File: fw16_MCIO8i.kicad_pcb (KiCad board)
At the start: 4 copper layers, 118.7 x 72.5 mm, 12 parts

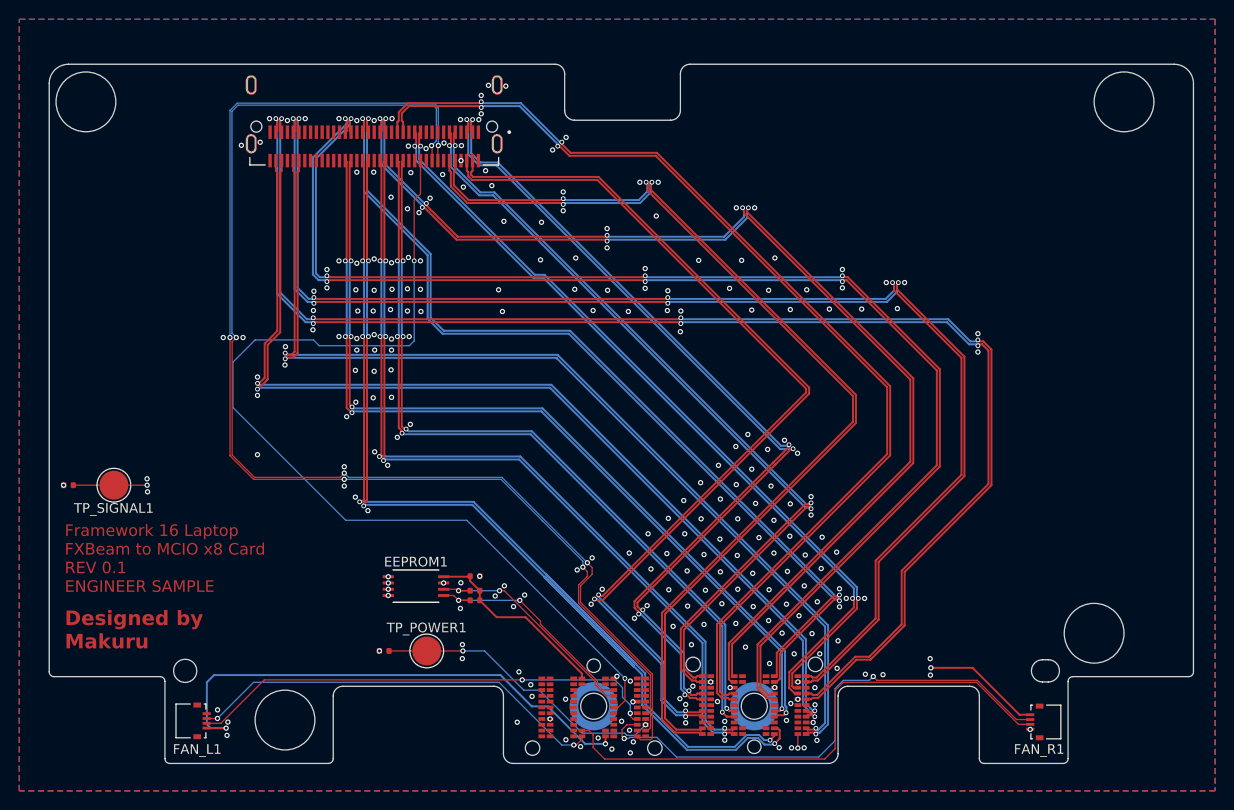
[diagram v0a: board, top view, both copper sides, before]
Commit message: Removed pour on signal layers
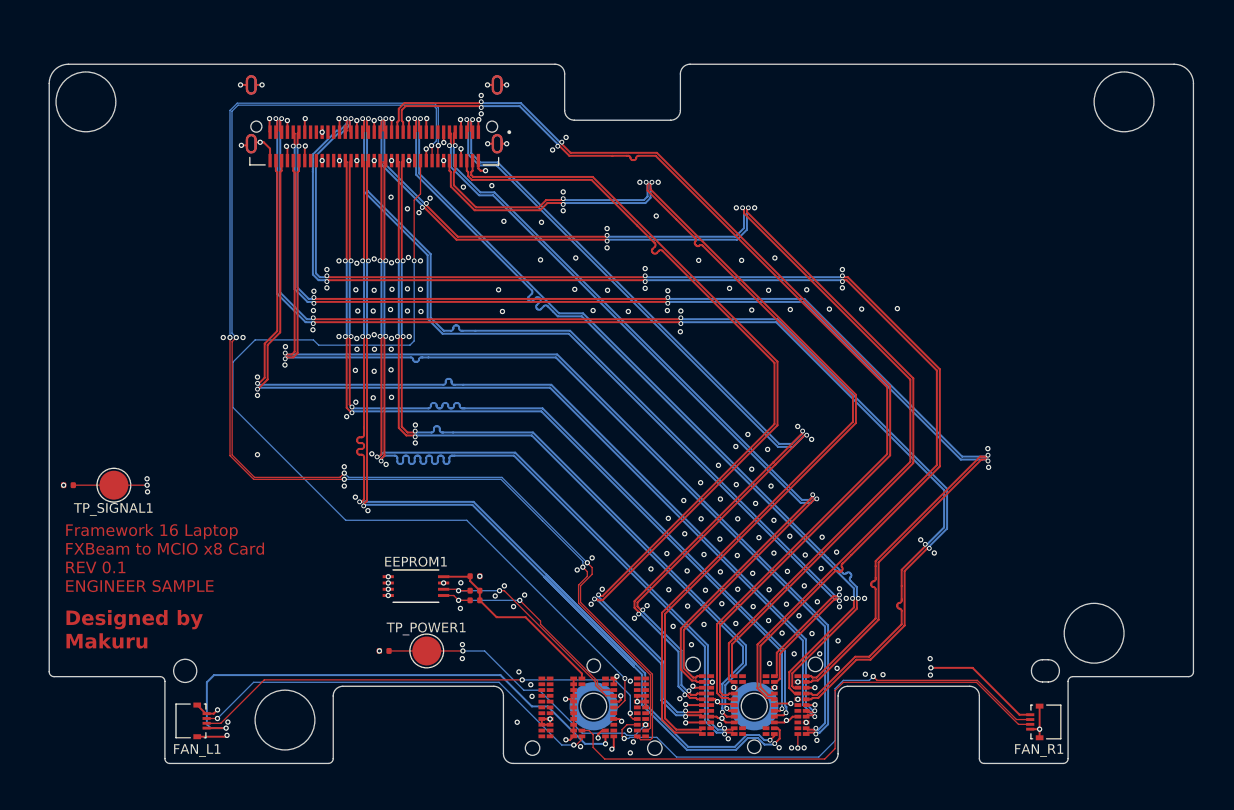
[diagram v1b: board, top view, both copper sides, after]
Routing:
- net GND: track 0.00 -> 80.4 mm, vias 263 -> 269
- net /RX7+: track 141.9 -> 126.9 mm
- net /RX7-: track 141.4 -> 126.9 mm
- net /RX6-: track 135.8 -> 127.9 mm
- net /TX3+: track 84.6 -> 91.4 mm
- net /PEX_CLK-: track 81.2 -> 88.1 mm
- net /RX6+: track 134.2 -> 127.9 mm
- net /PEX_CLK+: track 80.6 -> 84.9 mm
- net /RX0+: track 87.4 -> 91.4 mm
- net /RX0-: track 87.6 -> 91.4 mm
- net /TX0+: track 96.1 -> 93.1 mm
- net /TX2+: track 79.6 -> 82.3 mm
- net /TX5+: track 89.0 -> 91.0 mm
- net /TX4-: track 118.7 -> 120.6 mm
- net /TX0-: track 94.9 -> 93.0 mm
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- removed copper zone on B.Cu, net GND
- removed copper zone on F.Cu, net GND

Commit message: diodes and jumpers
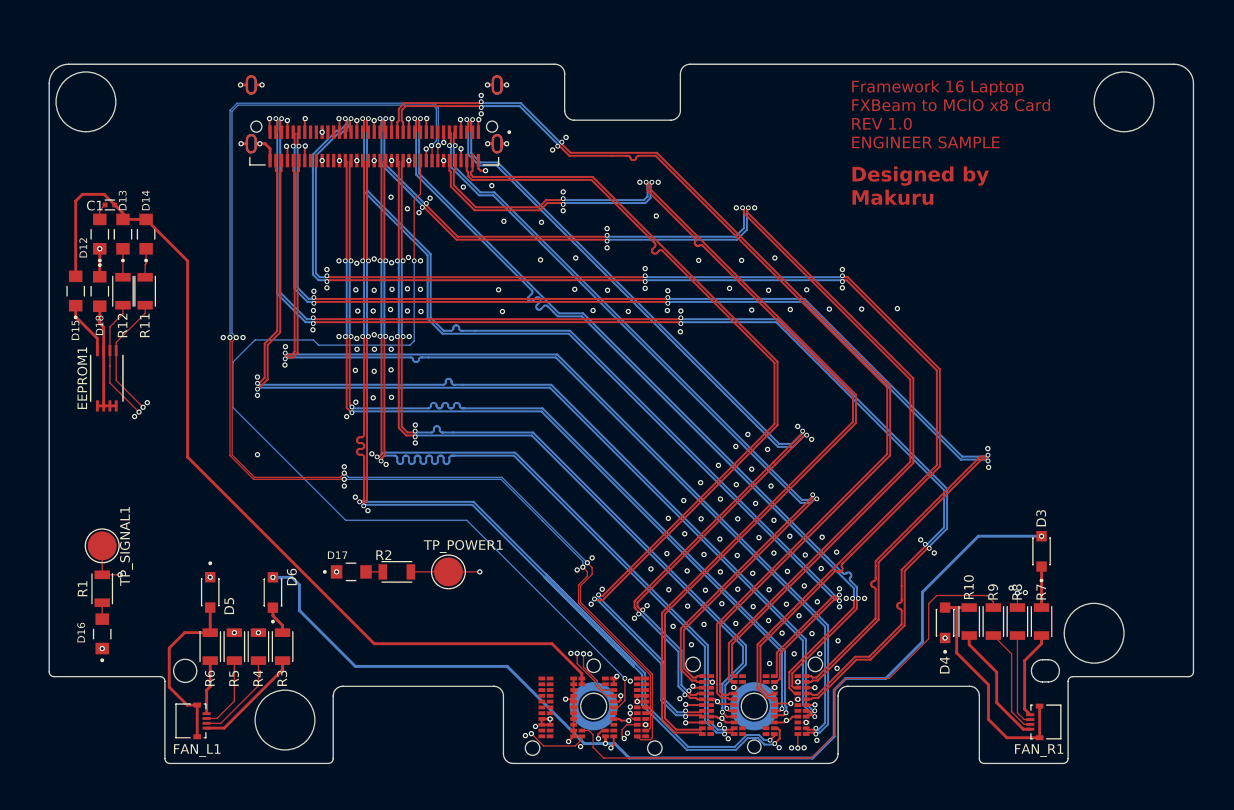
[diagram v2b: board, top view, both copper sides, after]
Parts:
- removed R50, R51: 10kΩ, PCM_JLCPCB:R_0402
- added D12: SS115LW, diode:DIO_SS115LW, F.Cu at (48.3, 42.3)
- added D13: SS115LW, diode:DIO_SS115LW, F.Cu at (50.7, 42.3)
- added D14: SS115LW, diode:DIO_SS115LW, F.Cu at (53.1, 42.3)
- added D15: SS115LW, diode:DIO_SS115LW, F.Cu at (45.8, 48.2)
- added D16: SS115LW, diode:DIO_SS115LW, F.Cu at (48.6, 83.8)
- added D17: SS115LW, diode:DIO_SS115LW, F.Cu at (74.4, 77.3)
- added D18: SS115LW, diode:DIO_SS115LW, F.Cu at (48.3, 48.2)
- added D3: ES15DLW, fan-diode:SODFL3718X102N, F.Cu at (146.0, 75.2)
- added D4: ES15DLW, fan-diode:SODFL3718X102N, F.Cu at (136.0, 82.6)
- added D5: ES15DLW, fan-diode:SODFL3718X102N, F.Cu at (59.8, 79.4)
- added D6: ES15DLW, fan-diode:SODFL3718X102N, F.Cu at (66.3, 79.4)
- added R10: 1206_R_560112132007, resistors:R_Wurth_WRIS-RSKS-1206_R, F.Cu at (138.5, 82.5)
- added R11: 1206_R_560112132018, resistors:R_Wurth_WRIS-RSKS-1206_R, F.Cu at (53.0, 48.2)
- added R12: 1206_R_560112132018, resistors:R_Wurth_WRIS-RSKS-1206_R, F.Cu at (50.7, 48.2)
- added R3: 1206_R_560112132007, resistors:R_Wurth_WRIS-RSKS-1206_R, F.Cu at (67.3, 85.0)
- added R4: 1206_R_560112132007, resistors:R_Wurth_WRIS-RSKS-1206_R, F.Cu at (64.8, 85.0)
- added R5: 1206_R_560112132007, resistors:R_Wurth_WRIS-RSKS-1206_R, F.Cu at (62.3, 85.0)
- added R6: 1206_R_560112132007, resistors:R_Wurth_WRIS-RSKS-1206_R, F.Cu at (59.8, 85.0)
- added R7: 1206_R_560112132007, resistors:R_Wurth_WRIS-RSKS-1206_R, F.Cu at (146.0, 82.5)
- added R8: 1206_R_560112132007, resistors:R_Wurth_WRIS-RSKS-1206_R, F.Cu at (143.5, 82.5)
- added R9: 1206_R_560112132007, resistors:R_Wurth_WRIS-RSKS-1206_R, F.Cu at (141.0, 82.5)
- C1: value 1uF -> 0402_885012105012; footprint PCM_JLCPCB:C_0402 -> capacitor:C_Wurth_WCAP-CSGP-0402
- R1: renamed from R2; value 330kΩ -> 1206_R_560112132036; footprint PCM_JLCPCB:R_0402 -> resistors:R_Wurth_WRIS-RSKS-1206_R
- R2: renamed from R1; value 330kΩ -> 1206_R_560112132036; footprint PCM_JLCPCB:R_0402 -> resistors:R_Wurth_WRIS-RSKS-1206_R
- moved C1 54.0 mm to (49.4, 39.2), turned to 180 degrees
- moved EEPROM1 38.6 mm to (49.1, 57.2), turned to 90 degrees
- moved R1 11.3 mm to (48.6, 79.0), turned to 90 degrees
- moved TP_POWER1 8.50 mm to (84.5, 77.3)
- moved R2 8.30 mm to (79.2, 77.3)
- moved TP_SIGNAL1 6.41 mm to (48.6, 74.6), turned to -90 degrees
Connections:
- C1 pad 2: GND -> Net-(C1-Pad2)
- EEPROM1 pad 1: GND -> Net-(EEPROM1-E0)
- EEPROM1 pad 2: GND -> Net-(EEPROM1-E0)
- EEPROM1 pad 3: GND -> Net-(EEPROM1-E0)
- EEPROM1 pad 4: GND -> Net-(EEPROM1-E0)
- EEPROM1 pad 7: GND -> Net-(EEPROM1-E0)
- EEPROM1 pad 8: 3V3_ALW -> Net-(EEPROM1-VCC)
- FAN_L1 pad 1: GND -> Net-(FAN_L1-Pad1)
- FAN_L1 pad 2: /FAN0_PWM -> Net-(FAN_L1-Pad2)
- FAN_L1 pad 3: /FAN0_SPD -> Net-(FAN_L1-Pad3)
- FAN_L1 pad 4: 12V_FAN -> Net-(FAN_L1-Pad4)
- FAN_L1 pad SH1: GND -> Net-(D5-PadA)
- FAN_L1 pad SH2: GND -> Net-(D5-PadA)
- FAN_R1 pad 1: GND -> Net-(FAN_R1-Pad1)
- FAN_R1 pad 2: /FAN1_PWM -> Net-(FAN_R1-Pad2)
- FAN_R1 pad 3: /FAN1_SPD -> Net-(FAN_R1-Pad3)
- FAN_R1 pad 4: 12V_FAN -> Net-(FAN_R1-Pad4)
- FAN_R1 pad SH1: GND -> Net-(D4-PadA)
- FAN_R1 pad SH2: GND -> Net-(D4-PadA)
- R1 pad 1: GND -> Net-(D16-PadA)
- R2 pad 1: GND -> Net-(D17-PadA)
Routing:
- net 3V3_ALW: track 19.4 -> 94.6 mm
- net /I2C_SDA: track 23.3 -> 75.3 mm
- net /I2C_SCL: track 23.6 -> 75.4 mm
- net Net-(D4-PadA): track 0.00 -> 24.8 mm
- net Net-(D5-PadA): track 0.00 -> 18.5 mm
- net Net-(FAN_R1-Pad1): track 0.00 -> 12.8 mm
- net Net-(EEPROM1-E0): track 0.00 -> 12.5 mm
- net Net-(FAN_L1-Pad4): track 0.00 -> 11.3 mm
- net Net-(FAN_R1-Pad2): track 0.00 -> 11.2 mm
- net Net-(FAN_R1-Pad3): track 0.00 -> 9.62 mm
- net Net-(FAN_L1-Pad3): track 0.00 -> 9.59 mm
- net Net-(FAN_R1-Pad4): track 0.00 -> 9.17 mm
- net Net-(FAN_L1-Pad2): track 0.00 -> 7.82 mm
- net GND: track 80.4 -> 73.6 mm, vias 269 -> 251
- net Net-(IN1-ID1): track 97.7 -> 91.0 mm
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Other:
- board text added: "Framework 16 Laptop FXBeam to MCIO x8 Card REV 1.0 ENGINEER SAMPLE"
- board text removed: "Framework 16 Laptop FXBeam to MCIO x8 Card REV 0.1 ENGINEER SAMPLE"

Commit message: README and cleanup
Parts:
- removed D12, D13, D14, D15, D18: SS115LW, diode:DIO_SS115LW
- moved C1 13.8 mm to (47.6, 53.0)
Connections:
- C1 pad 2: Net-(C1-Pad2) -> GND
- EEPROM1 pad 1: Net-(EEPROM1-E0) -> GND
- EEPROM1 pad 2: Net-(EEPROM1-E0) -> GND
- EEPROM1 pad 3: Net-(EEPROM1-E0) -> GND
- EEPROM1 pad 4: Net-(EEPROM1-E0) -> GND
- EEPROM1 pad 7: Net-(EEPROM1-E0) -> GND
- EEPROM1 pad 8: Net-(EEPROM1-VCC) -> 3V3_ALW
- R11 pad 2: Net-(D14-PadC) -> 3V3_ALW
- R12 pad 2: Net-(D13-PadC) -> 3V3_ALW
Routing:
- net GND: track 73.6 -> 115.7 mm, vias 251 -> 239
- net /TX4+: track 120.7 -> 98.8 mm
- net /TX4-: track 120.6 -> 100.8 mm
- net Net-(EEPROM1-E0): track 12.5 -> 0.00 mm
- net /TX3+: track 91.4 -> 85.2 mm
- net Net-(EEPROM1-VCC): track 5.83 -> 0.00 mm
- net /I2C_SDA: track 75.3 -> 80.3 mm
- net /I2C_SCL: track 75.4 -> 79.8 mm
- net /TX5-: track 88.3 -> 91.7 mm
- net Net-(D14-PadC): track 2.99 -> 0.00 mm
- net /PEX_CLK-: track 88.1 -> 85.1 mm
- net Net-(D13-PadC): track 2.95 -> 0.00 mm
- net 12V_FAN: track 105.1 -> 107.0 mm
- net Net-(C1-Pad2): track 1.73 -> 0.00 mm
- net /TX2+: track 82.3 -> 83.6 mm
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
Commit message: Skewing around
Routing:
- net /TX4-: track 100.8 -> 99.4 mm
- net /TX4+: track 98.8 -> 99.4 mm
- net /RX4+: track 91.9 -> 91.2 mm
- net /PEX_CLK+: track 84.2 -> 84.8 mm
- net GND: vias 239 -> 249

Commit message: MPN added and removed unedded diode
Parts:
- removed D4, D5: ES15DLW, fan-diode:SODFL3718X102N
- FAN_L1, FAN_R1: value F3011B7H111005E200 -> F3311A7H121004E200; footprint fan-connector:AMPHENOL_F33D-1A7H1-E7C04 -> fan-connector:AMPHENOL_F3311A7H121004E200
- moved D6 8.33 mm to (58.2, 81.5), turned to 0 degrees
- moved D3 4.44 mm to (141.7, 76.4), turned to 180 degrees
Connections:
- D3 pad A: 12V_FAN -> Net-(D3-PadA)
- D3 pad C: Net-(D3-PadC) -> GND
- D6 pad A: 12V_FAN -> Net-(D6-PadA)
- D6 pad C: Net-(D6-PadC) -> GND
- FAN_L1 pad SH1: Net-(D5-PadA) -> (no net)
- FAN_L1 pad SH2: Net-(D5-PadA) -> (no net)
- FAN_R1 pad SH1: Net-(D4-PadA) -> (no net)
- FAN_R1 pad SH2: Net-(D4-PadA) -> (no net)
- R10 pad 2: Net-(D4-PadA) -> Net-(D3-PadA)
- R3 pad 2: Net-(D6-PadC) -> 12V_FAN
- R6 pad 2: Net-(D5-PadA) -> Net-(D6-PadA)
- R7 pad 2: Net-(D3-PadC) -> 12V_FAN
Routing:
- net Net-(D4-PadA): track 24.8 -> 0.00 mm
- net Net-(D5-PadA): track 18.5 -> 0.00 mm
- net Net-(D3-PadA): track 0.00 -> 5.29 mm
- net GND: track 115.7 -> 120.5 mm, vias 249 -> 251
- net Net-(D3-PadC): track 4.25 -> 0.00 mm
- net 12V_FAN: track 107.0 -> 111.1 mm
- net Net-(D6-PadC): track 3.00 -> 0.00 mm
- net /FAN1_PWM: track 57.4 -> 59.5 mm, vias 0 -> 2
- net Net-(D6-PadA): track 0.00 -> 2.10 mm

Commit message: Switched capacitor
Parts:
- C1: value 0402_885012105012 -> 1206_H1.6_885012208018; footprint capacitor:C_Wurth_WCAP-CSGP-0402 -> capacitor:C_Wurth_WCAP-CSGP-1206_H0.8
- moved C1 2.13 mm to (46.5, 51.1)
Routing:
- net GND: track 120.5 -> 123.7 mm
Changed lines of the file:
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@@
 		)
 	)
-	(footprint "capacitor:C_Wurth_WCAP-CSGP-0402"
+	(footprint "capacitor:C_Wurth_WCAP-CSGP-1206_H0.8"
 		(layer "F.Cu")
-		(at 47.6 52.95 180)
-		(descr "MLCCs General Purpose, body 1x0.5x0.5mm, https://www.we-online.com/en/components/products/WCAP-CSGP-6_3VDC")
+		(at 46.55 51.1 180)
+		(descr "MLCCs General Purpose, body 3.2x1.6x0.8mm, https://www.we-online.com/en/components/products/WCAP-CSGP-6_3VDC")
 		(tags "SMT")
 		(property "Reference" "C1"
-			(at 1.55 -0.1 0)
+			(at 1.5 1.7 0)
 			(unlocked yes)
 			(layer "F.SilkS")
@@
 			)
 		)
-		(property "Value" "0402_885012105012"
-			(at 0 1.4 180)
+		(property "Value" "1206_H1.6_885012208018"
+			(at 0 2.05 180)
 			(unlocked yes)
 			(layer "F.Fab")
@@
 			)
 		)
-		(property "Datasheet" "https://www.we-online.com/catalog/datasheet/885012105012.pdf?ki"
+		(property "Datasheet" "https://www.we-online.com/catalog/datasheet/885012208018.pdf?ki"
 			(at 0 0 0)
 			(layer "F.Fab")
@@
 			)
 		)
-		(property "Size" "0402"
+		(property "Size" "1206_H1.6"
 			(at 0 0 180)
 			(unlocked yes)
@@
 			)
 		)
-		(property "Part Number" "885012105012"
+		(property "Part Number" "885012208018"
 			(at 0 0 180)
 			(unlocked yes)
@@
 			)
 		)
-		(property "Capacitance" "1 µF"
+		(property "Capacitance" "10 µF"
 			(at 0 0 180)
 			(unlocked yes)
@@
 			)
 		)
-		(property "C" "1 µF"
+		(property "C" "10 µF"
 			(at 0 0 180)
 			(unlocked yes)
@@
 			)
 		)
-		(property "Tol. C" "±20%"
+		(property "Tol. C" "±10%"
 			(at 0 0 180)
 			(unlocked yes)
@@
 			)
 		)
-		(property "Operating Temperature" "-55 °C up to +85 °C"
+		(property "Operating Temperature" "-55 °C up to +125 °C"
 			(at 0 0 180)
 			(unlocked yes)
@@
 			)
 		)
-		(property "DF (%)" "15"
+		(property "DF (%)" "10"
 			(at 0 0 180)
 			(unlocked yes)
@@
 			)
 		)
-		(property "RISO" "0.05 GΩ"
+		(property "RISO" "0.01 GΩ"
 			(at 0 0 180)
 			(unlocked yes)
@@
 			)
 		)
-		(property "Ceramic Type" "X5R Class II"
+		(property "Ceramic Type" "X7R Class II"
 			(at 0 0 180)
 			(unlocked yes)
@@
 			)
 		)
-		(property "L (mm)" "1.0"
+		(property "L (mm)" "3.2"
 			(at 0 0 180)
 			(unlocked yes)
@@
 			)
 		)
-		(property "W (mm)" "0.5"
+		(property "W (mm)" "1.6"
 			(at 0 0 180)
 			(unlocked yes)
@@
 			)
 		)
-		(property "H (mm)" "0.5"
+		(property "H (mm)" "1.6"
 			(at 0 0 180)
 			(unlocked yes)
@@
 			)
 		)
-		(property "Fl (mm)" "0.25"
+		(property "Fl (mm)" "0.6"
 			(at 0 0 180)
 			(unlocked yes)
@@
 			)
 		)
-		(property "MPN" "885012105012"
-			(at 0 0 180)
-			(unlocked yes)
-			(layer "F.Fab")
-			(hide yes)
-			(effects
-				(font
-					(size 1 1)
-					(thickness 0.15)
-				)
-			)
-		)
-		(property "LCSC Part #" "C6476410"
-			(at 0 0 180)
-			(unlocked yes)
-			(layer "F.Fab")
-			(hide yes)
-			(effects
-				(font
-					(size 1 1)
-					(thickness 0.15)
-				)
-			)
-		)
-		(property ki_fp_filters "*WCAP-CSGP*0402*")
+		(property ki_fp_filters "*WCAP-CSGP*1206*")
 		(sheetname "/")
 		(sheetfile "fw16_MCIO8i.kicad_sch")
 		(attr smd)
 		(fp_line
-			(start -0.5 0.51)
-			(end 0.5 0.51)
+			(start -1.6 1.06)
+			(end 1.6 1.06)
 			(stroke
 				(width 0.12)
@@
 		)
 		(fp_line
-			(start -0.5 -0.51)
-			(end 0.5 -0.51)
+			(start -1.6 -1.06)
+			(end 1.6 -1.06)
 			(stroke
 				(width 0.12)
@@
 		)
 		(fp_rect
-			(start -0.9 -0.4)
-			(end 0.9 0.4)
+			(start -2.25 -1.05)
+			(end 2.25 1.05)
 			(stroke
 				(width 0.05)
@@
 		)
 		(fp_rect
-			(start -0.5 -0.25)
-			(end 0.5 0.25)
+			(start -1.6 -0.8)
+			(end 1.6 0.8)
 			(stroke
 				(width 0.1)
@@
 		)
 		(pad "1" smd rect
-			(at -0.5 0 180)
-			(size 0.5 0.5)
+			(at -1.55 0 180)
+			(size 0.9 1.6)
 			(layers "F.Cu" "F.Mask" "F.Paste")
 			(net 34 "3V3_ALW")
@@
 		)
 		(pad "2" smd rect
-			(at 0.5 0 180)
-			(size 0.5 0.5)
+			(at 1.55 0 180)
+			(size 0.9 1.6)
 			(layers "F.Cu" "F.Mask" "F.Paste")
 			(net 1 "GND")
@@
 		)
 		(embedded_fonts no)
-		(model "${KIPRJMOD}/components/capacitor/3dmodels/Capacitor_SMD_Wurth.3dshapes/C_Wurth_WCAP-CSGP-0402.wrl"
+		(model "${KIPRJMOD}/components/capacitor/3dmodels/Capacitor_SMD_Wurth.3dshapes/C_Wurth_WCAP-CSGP-1206_H0.8.wrl"
 			(offset
 				(xyz 0 0 0)
@@
 	)
 	(segment
+		(start 46.3 55.9)
+		(end 45 54.6)
+		(width 0.3)
+		(layer "F.Cu")
+		(net 1)
+	)
+	(segment
 		(start 89.554799 26.805557)
 		(end 88.55 26.805557)
@@
 	)
 	(segment
+		(start 45 54.6)
+		(end 45 51.1)
+		(width 0.3)
+		(layer "F.Cu")
+		(net 1)
+	)
+	(segment
 		(start 75.004799 30.504799)
 		(end 75 30.5)
@@
 	)
 	(segment
+		(start 47.1 55.9)
+		(end 46.3 55.9)
+		(width 0.3)
+		(layer "F.Cu")
+		(net 1)
+	)
+	(segment
 		(start 111.692214 90.511826)
 		(end 112.402403 90.511826)
@@
 	)
 	(segment
-		(start 47.1 55.9)
-		(end 47.1 52.95)
-		(width 0.3)
-		(layer "F.Cu")
-		(net 1)
-	)
-	(segment
 		(start 104.082214 90.151826)
 		(end 104.942214 90.151826)
@@
 	)
 	(segment
-		(start 53.049972 46.75)
-		(end 55.075 46.75)
+		(start 48.1 54.349986)
+		(end 48.100014 54.35)
 		(width 0.3)
 		(layer "F.Cu")
@@
 	)
 	(segment
-		(start 55.075 46.75)
-		(end 57.45 49.125)
+		(start 53.049972 46.75)
+		(end 55.075 46.75)
 		(width 0.3)
 		(layer "F.Cu")
@@
 	)
 	(segment
-		(start 48.1 47.7)
-		(end 49.05 46.75)
+		(start 55.075 46.75)
+		(end 57.45 49.125)
 		(width 0.3)
 		(layer "F.Cu")
@@
 	)
 	(segment
-		(start 48.100014 52.950014)
-		(end 48.1 52.95)
+		(start 48.1 51.1)
+		(end 48.1 54.349986)
 		(width 0.3)
 		(layer "F.Cu")
@@
 	)
 	(segment
-		(start 48.100014 54.35)
-		(end 48.100014 52.950014)
-		(width 0.3)
-		(layer "F.Cu")
-		(net 34)
-	)
-	(segment
-		(start 48.1 52.95)
-		(end 48.1 47.7)
+		(start 48.1 47.7)
+		(end 49.05 46.75)
 		(width 0.3)
 		(layer "F.Cu")
@@
 		(width 0.3)
 		(layer "F.Cu")
+		(net 34)
+	)
+	(segment
+		(start 48.1 51.1)
+		(end 48.1 47.7)
+		(width 0.3)
+		(layer "F.Cu")
